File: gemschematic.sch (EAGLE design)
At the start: 15 parts, among them U7 STM32L073RZT6

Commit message: Add files via upload
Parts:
- added POWER: (no value), pinhead:PINHD-1X2
- added STLINK: 22-23-2041, con-molex:22-23-2041
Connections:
- removed net VDD: U7.VDD
- removed net VIN: BARO-1.S
- new net SWCLK: STLINK-3.S, U7.PA14
- new net SWIO: STLINK-2.S, U7.PA13
- net GND: now also POWER.2, STLINK-4.S
- net MISOLORA: now also U7.PA6; no longer U7.PC12
- net MOSILORA: now also U7.PA7; no longer U7.PC11
- net SCKLORA: now also U7.PA5; no longer U7.PC6
- net VCC: now also BARO-1.S, POWER.1, STLINK-1.S
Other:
- note added: "Stlink"
- moved on the sheet: DS18B20, PULLUP2
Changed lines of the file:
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@@
 <part name="BARO" library="con-molex" library_urn="urn:adsk.eagle:library:165" deviceset="22-23-2041" device="" package3d_urn="urn:adsk.eagle:package:8078635/1"/>
 <part name="GND6" library="supply1" library_urn="urn:adsk.eagle:library:371" deviceset="GND" device=""/>
+<part name="STLINK" library="con-molex" library_urn="urn:adsk.eagle:library:165" deviceset="22-23-2041" device="" package3d_urn="urn:adsk.eagle:package:8078635/1"/>
+<part name="POWER" library="pinhead" library_urn="urn:adsk.eagle:library:325" deviceset="PINHD-1X2" device="" package3d_urn="urn:adsk.eagle:package:22435/2"/>
 </parts>
 <sheets>
@@
 <text x="185.42" y="149.86" size="1.778" layer="91">Bluetooth Jumpers</text>
 <text x="241.3" y="-22.86" size="1.778" layer="91">version 3</text>
+<text x="205.74" y="55.88" size="1.778" layer="91">Stlink</text>
 </plain>
 <instances>
@@
 <attribute name="VALUE" x="-48.26" y="78.74" size="1.778" layer="96" rot="R270"/>
 </instance>
-<instance part="DS18B20" gate="A" x="-12.7" y="142.24" smashed="yes">
-<attribute name="NAME" x="-19.05" y="147.955" size="1.778" layer="95"/>
-<attribute name="VALUE" x="-19.05" y="134.62" size="1.778" layer="96"/>
-</instance>
-<instance part="GND4" gate="1" x="-33.02" y="139.7" smashed="yes" rot="R270">
-<attribute name="VALUE" x="-35.56" y="142.24" size="1.778" layer="96" rot="R270"/>
-</instance>
-<instance part="PULLUP2" gate="G$1" x="-38.1" y="144.78" smashed="yes" rot="R90">
-<attribute name="NAME" x="-39.5986" y="140.97" size="1.778" layer="95" rot="R90"/>
-<attribute name="VALUE" x="-34.798" y="140.97" size="1.778" layer="96" rot="R90"/>
-<attribute name="PULLUP" x="-38.1" y="144.78" size="1.778" layer="96" rot="R90" display="off"/>
+<instance part="DS18B20" gate="A" x="17.78" y="139.7" smashed="yes">
+<attribute name="NAME" x="11.43" y="145.415" size="1.778" layer="95"/>
+<attribute name="VALUE" x="11.43" y="132.08" size="1.778" layer="96"/>
+</instance>
+<instance part="GND4" gate="1" x="-2.54" y="137.16" smashed="yes" rot="R270">
+<attribute name="VALUE" x="-5.08" y="139.7" size="1.778" layer="96" rot="R270"/>
+</instance>
+<instance part="PULLUP2" gate="G$1" x="-7.62" y="142.24" smashed="yes" rot="R90">
+<attribute name="NAME" x="-9.1186" y="138.43" size="1.778" layer="95" rot="R90"/>
+<attribute name="VALUE" x="-4.318" y="138.43" size="1.778" layer="96" rot="R90"/>
+<attribute name="PULLUP" x="-7.62" y="142.24" size="1.778" layer="96" rot="R90" display="off"/>
 </instance>
 <instance part="BLUETOOTH" gate="-1" x="205.74" y="139.7" smashed="yes">
@@
 <instance part="GND6" gate="1" x="154.94" y="45.72" smashed="yes" rot="R270">
 <attribute name="VALUE" x="152.4" y="48.26" size="1.778" layer="96" rot="R270"/>
+</instance>
+<instance part="STLINK" gate="-1" x="215.9" y="48.26" smashed="yes">
+<attribute name="NAME" x="218.44" y="47.498" size="1.524" layer="95"/>
+</instance>
+<instance part="STLINK" gate="-2" x="215.9" y="45.72" smashed="yes">
+<attribute name="NAME" x="218.44" y="44.958" size="1.524" layer="95"/>
+</instance>
+<instance part="STLINK" gate="-3" x="215.9" y="43.18" smashed="yes">
+<attribute name="NAME" x="218.44" y="42.418" size="1.524" layer="95"/>
+</instance>
+<instance part="STLINK" gate="-4" x="215.9" y="40.64" smashed="yes">
+<attribute name="NAME" x="218.44" y="39.878" size="1.524" layer="95"/>
+</instance>
+<instance part="POWER" gate="G$1" x="167.64" y="12.7" smashed="yes">
+<attribute name="NAME" x="161.29" y="18.415" size="1.778" layer="95"/>
+<attribute name="VALUE" x="161.29" y="7.62" size="1.778" layer="96"/>
 </instance>
 </instances>
@@
 <segment>
 <pinref part="DS18B20" gate="A" pin="1"/>
-<wire x1="-15.24" y1="144.78" x2="-30.48" y2="144.78" width="0.1524" layer="91"/>
-<label x="-30.48" y="144.78" size="1.778" layer="95"/>
-<wire x1="-30.48" y1="144.78" x2="-30.48" y2="149.86" width="0.1524" layer="91"/>
-<wire x1="-30.48" y1="149.86" x2="-38.1" y2="149.86" width="0.1524" layer="91"/>
+<wire x1="15.24" y1="142.24" x2="0" y2="142.24" width="0.1524" layer="91"/>
+<label x="0" y="142.24" size="1.778" layer="95"/>
+<wire x1="0" y1="142.24" x2="0" y2="147.32" width="0.1524" layer="91"/>
+<wire x1="0" y1="147.32" x2="-7.62" y2="147.32" width="0.1524" layer="91"/>
 <pinref part="PULLUP2" gate="G$1" pin="2"/>
-<wire x1="-38.1" y1="149.86" x2="-43.18" y2="149.86" width="0.1524" layer="91"/>
-<junction x="-38.1" y="149.86"/>
+<wire x1="-7.62" y1="147.32" x2="-12.7" y2="147.32" width="0.1524" layer="91"/>
+<junction x="-7.62" y="147.32"/>
 </segment>
 <segment>
@@
 <wire x1="203.2" y1="132.08" x2="187.96" y2="132.08" width="0.1524" layer="91"/>
 <label x="187.96" y="132.08" size="1.778" layer="95"/>
+</segment>
+<segment>
+<pinref part="STLINK" gate="-1" pin="S"/>
+<wire x1="213.36" y1="48.26" x2="205.74" y2="48.26" width="0.1524" layer="91"/>
+<label x="205.74" y="48.26" size="1.778" layer="95"/>
+</segment>
+<segment>
+<pinref part="BARO" gate="-1" pin="S"/>
+<wire x1="167.64" y1="48.26" x2="157.48" y2="48.26" width="0.1524" layer="91"/>
+<label x="157.48" y="48.26" size="1.778" layer="95"/>
+</segment>
+<segment>
+<pinref part="POWER" gate="G$1" pin="1"/>
+<wire x1="165.1" y1="15.24" x2="154.94" y2="15.24" width="0.1524" layer="91"/>
+<label x="154.94" y="15.24" size="1.778" layer="95"/>
 </segment>
 </net>
@@
 <segment>
 <pinref part="DS18B20" gate="A" pin="3"/>
-<wire x1="-15.24" y1="139.7" x2="-30.48" y2="139.7" width="0.1524" layer="91"/>
+<wire x1="15.24" y1="137.16" x2="0" y2="137.16" width="0.1524" layer="91"/>
 <pinref part="GND4" gate="1" pin="GND"/>
 </segment>
@@
 <wire x1="167.64" y1="45.72" x2="157.48" y2="45.72" width="0.1524" layer="91"/>
 <pinref part="GND6" gate="1" pin="GND"/>
+</segment>
+<segment>
+<pinref part="STLINK" gate="-4" pin="S"/>
+<wire x1="213.36" y1="40.64" x2="205.74" y2="40.64" width="0.1524" layer="91"/>
+<label x="205.74" y="40.64" size="1.778" layer="95"/>
+</segment>
+<segment>
+<pinref part="POWER" gate="G$1" pin="2"/>
+<wire x1="165.1" y1="12.7" x2="154.94" y2="12.7" width="0.1524" layer="91"/>
+<label x="154.94" y="12.7" size="1.778" layer="95"/>
 </segment>
 </net>
@@
 </segment>
 </net>
-<net name="VDD" class="0">
-<segment>
-<pinref part="U7" gate="G$1" pin="VDD"/>
-<wire x1="96.52" y1="139.7" x2="111.76" y2="139.7" width="0.1524" layer="91"/>
-<label x="106.68" y="139.7" size="1.778" layer="95"/>
-</segment>
-</net>
 <net name="PA0LDR" class="0">
 <segment>
@@
 </segment>
 <segment>
-<pinref part="U7" gate="G$1" pin="PC6"/>
-<wire x1="96.52" y1="101.6" x2="111.76" y2="101.6" width="0.1524" layer="91"/>
-<label x="106.68" y="101.6" size="1.778" layer="95"/>
+<pinref part="U7" gate="G$1" pin="PA5"/>
+<wire x1="45.72" y1="104.14" x2="30.48" y2="104.14" width="0.1524" layer="91"/>
+<label x="30.48" y="104.14" size="1.778" layer="95"/>
 </segment>
 </net>
@@
 </segment>
 <segment>
-<pinref part="U7" gate="G$1" pin="PC12"/>
-<wire x1="96.52" y1="86.36" x2="111.76" y2="86.36" width="0.1524" layer="91"/>
-<label x="106.68" y="86.36" size="1.778" layer="95"/>
+<pinref part="U7" gate="G$1" pin="PA6"/>
+<wire x1="45.72" y1="101.6" x2="30.48" y2="101.6" width="0.1524" layer="91"/>
+<label x="30.48" y="101.6" size="1.778" layer="95"/>
 </segment>
 </net>
@@
 </segment>
 <segment>
-<pinref part="U7" gate="G$1" pin="PC11"/>
-<wire x1="96.52" y1="88.9" x2="111.76" y2="88.9" width="0.1524" layer="91"/>
-<label x="106.68" y="88.9" size="1.778" layer="95"/>
+<pinref part="U7" gate="G$1" pin="PA7"/>
+<wire x1="45.72" y1="99.06" x2="30.48" y2="99.06" width="0.1524" layer="91"/>
+<label x="30.48" y="99.06" size="1.778" layer="95"/>
 </segment>
 </net>
@@
 <segment>
 <pinref part="DS18B20" gate="A" pin="2"/>
-<wire x1="-15.24" y1="142.24" x2="-35.56" y2="142.24" width="0.1524" layer="91"/>
-<label x="-30.48" y="142.24" size="1.778" layer="95"/>
-<wire x1="-35.56" y1="142.24" x2="-35.56" y2="139.7" width="0.1524" layer="91"/>
+<wire x1="15.24" y1="139.7" x2="-5.08" y2="139.7" width="0.1524" layer="91"/>
+<label x="0" y="139.7" size="1.778" layer="95"/>
+<wire x1="-5.08" y1="139.7" x2="-5.08" y2="137.16" width="0.1524" layer="91"/>
 <pinref part="PULLUP2" gate="G$1" pin="1"/>
-<wire x1="-35.56" y1="139.7" x2="-38.1" y2="139.7" width="0.1524" layer="91"/>
-<wire x1="-38.1" y1="139.7" x2="-43.18" y2="139.7" width="0.1524" layer="91"/>
-<junction x="-38.1" y="139.7"/>
+<wire x1="-5.08" y1="137.16" x2="-7.62" y2="137.16" width="0.1524" layer="91"/>
+<wire x1="-7.62" y1="137.16" x2="-12.7" y2="137.16" width="0.1524" layer="91"/>
+<junction x="-7.62" y="137.16"/>
 </segment>
 <segment>
@@
 </segment>
 </net>
-<net name="VIN" class="0">
-<segment>
-<pinref part="BARO" gate="-1" pin="S"/>
-<wire x1="167.64" y1="48.26" x2="157.48" y2="48.26" width="0.1524" layer="91"/>
-<label x="157.48" y="48.26" size="1.778" layer="95"/>
-</segment>
-</net>
+<net name="SWIO" class="0">
+<segment>
+<pinref part="U7" gate="G$1" pin="PA13"/>
+<wire x1="45.72" y1="83.82" x2="30.48" y2="83.82" width="0.1524" layer="91"/>
+<label x="30.48" y="83.82" size="1.778" layer="95"/>
+</segment>
+<segment>
+<pinref part="STLINK" gate="-2" pin="S"/>
+<wire x1="213.36" y1="45.72" x2="205.74" y2="45.72" width="0.1524" layer="91"/>
+<label x="205.74" y="45.72" size="1.778" layer="95"/>
+</segment>
+</net>
+<net name="SWCLK" class="0">
+<segment>
+<pinref part="U7" gate="G$1" pin="PA14"/>
+<wire x1="45.72" y1="81.28" x2="30.48" y2="81.28" width="0.1524" layer="91"/>
+<label x="30.48" y="81.28" size="1.778" layer="95"/>
+</segment>
+<segment>
+<pinref part="STLINK" gate="-3" pin="S"/>
+<wire x1="213.36" y1="43.18" x2="205.74" y2="43.18" width="0.1524" layer="91"/>
+<label x="205.74" y="43.18" size="1.778" layer="95"/>
+</segment>
+</net>

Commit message: Add files via upload
added butons
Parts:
- added LEDRESISTOR: 510 Ohm, adafruit:R-US_0204/2V
- added RESETBUTTON, USERBUTTON: (no value), adafruit:40-XX
- added USERLED: (no value), adafruit:LED3MM
- BLUETOOTH: value 87438-06 -> (none); device con-molex:87438-06 -> adafruit:PINHD-1X6
- STLINK: value 22-23-2041 -> (none); device con-molex:22-23-2041 -> adafruit:PINHD-1X6
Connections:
- removed net !RESET: GPS1JUMPER.6
- removed net 3.3V: GPS1JUMPER.2
- removed net ANT: LORANT.1
- removed net IO18: LORA2JUMPER.5
- removed net IO19: LORA2JUMPER.6
- removed net IO23: LORA2JUMPER.7
- removed net IO25: LORA1JUMPER.5
- removed net IO27: LORA1JUMPER.4
- removed net IO4: LORA2JUMPER.3
- removed net IO5: LORA2JUMPER.4
- removed net MISOLORA: LORA1JUMPER.2, U7.PA6
- removed net MOSILORA: LORA1JUMPER.1, U7.PA7
- removed net RESET: LORA1JUMPER.6
- removed net RXI: LORA2JUMPER.8
- removed net SCKLORA: LORA1JUMPER.3, U7.PA5
- removed net SCL: LORA2JUMPER.2
- removed net SDA: LORA2JUMPER.1
- removed net SWCLK: STLINK-3.S, U7.PA14
- removed net SWIO: STLINK-2.S, U7.PA13
- removed net TXO: LORA2JUMPER.9
- removed net WAKEUP: GPS2JUMPER.6
- new net LED: LEDRESISTOR.2, U7.PA5
- new net N$1: LEDRESISTOR.1, USERLED.C
- new net NRST: RESETBUTTON.P, RESETBUTTON.P1, STLINK.5, U7.NRST
- new net SWCLKSTLINK: STLINK.2, U7.PA14
- new net SWDIOSTLINK: STLINK.4, U7.PA13
- new net SWOSTLINK: STLINK.6, U7.PB3
- new net USERBUTTON: U7.PC13, USERBUTTON.P, USERBUTTON.P1
- net BTRX: now also BLUETOOTH.2; no longer BLUETOOTH-2.S
- net BTTX: now also BLUETOOTH.3; no longer BLUETOOTH-3.S
- net GND: now also BLUETOOTH.5, RESETBUTTON.S, RESETBUTTON.S1, STLINK.3, U7.BOOT0, USERBUTTON.S, USERBUTTON.S1; no longer BLUETOOTH-5.S, STLINK-4.S
- net VCC: now also BLUETOOTH.4; no longer BLUETOOTH-4.S, STLINK-1.S
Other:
- note added: "LED"
- note added: "Power"

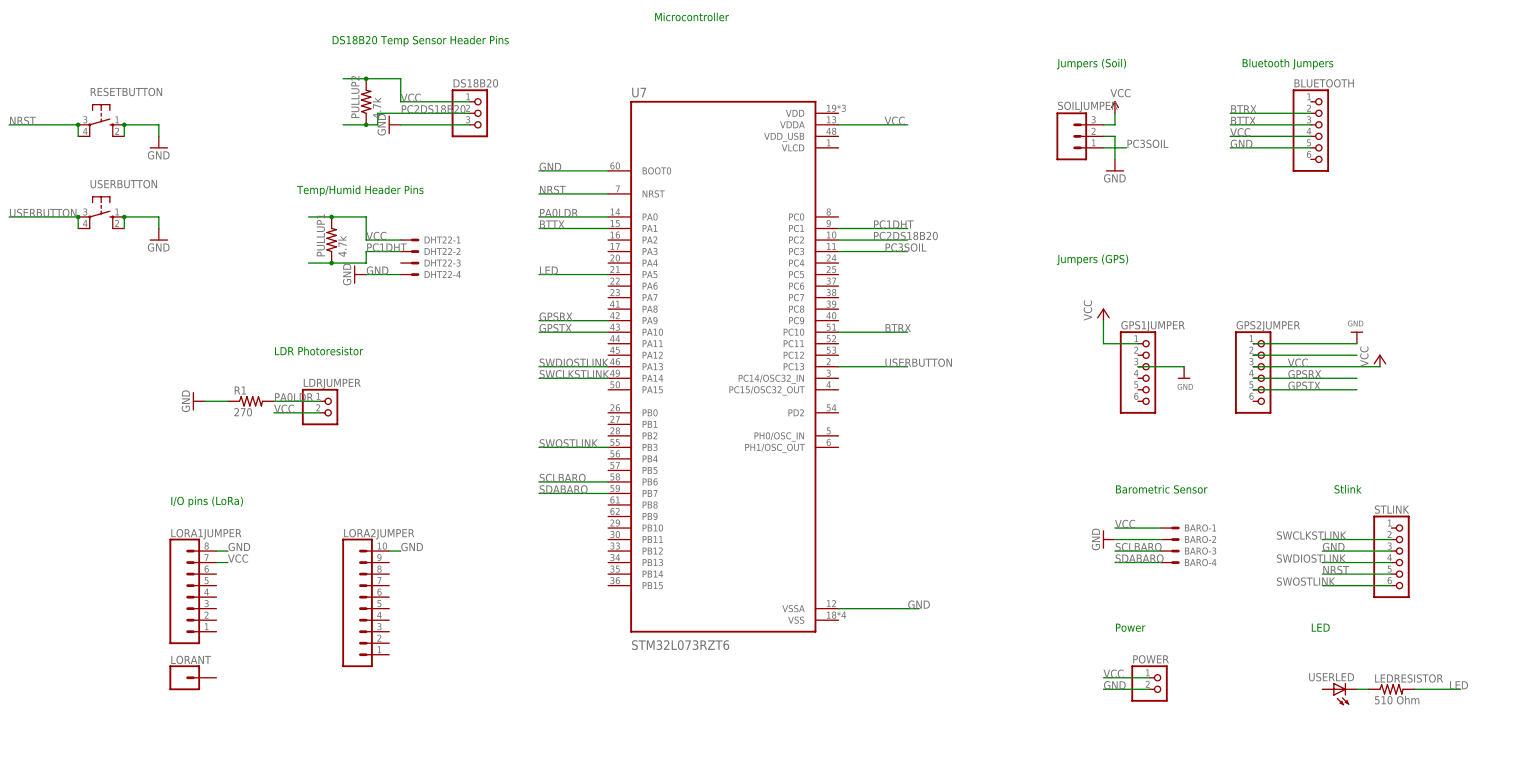
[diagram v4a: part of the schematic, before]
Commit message: added smd parts
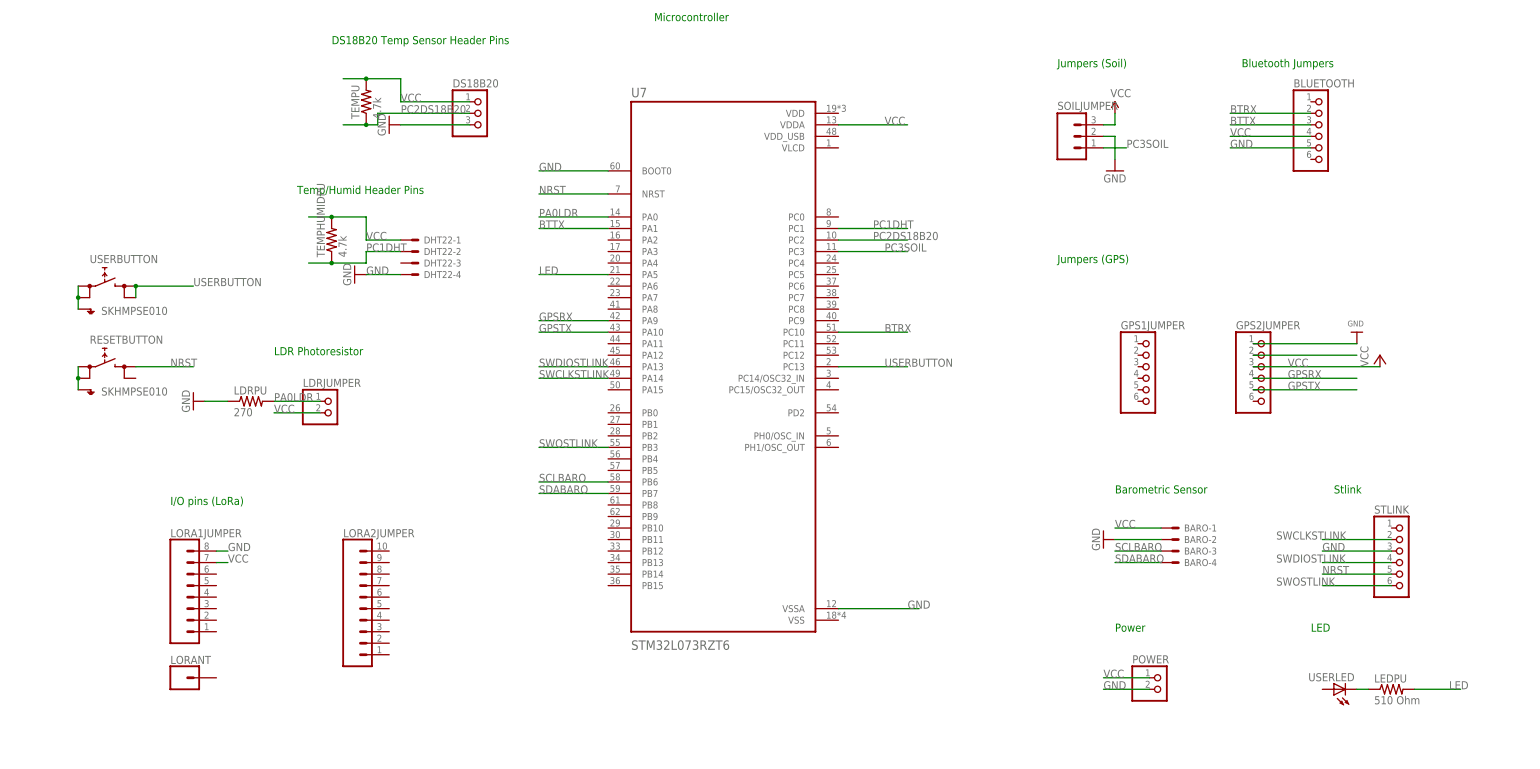
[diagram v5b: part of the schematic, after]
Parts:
- removed LEDRESISTOR: 510 Ohm, adafruit:R-US_0204/2V
- removed PULLUP1, PULLUP2: 4.7k, adafruit:R-US_0204/2V
- removed R1: 270, adafruit:R-US_0204/2V
- added LDRPU: 270, adafruit:R-US_M0805
- added LEDPU: 510 Ohm, adafruit:R-US_M0805
- added TEMPHUMIDPU, TEMPU: 4.7k, adafruit:R-US_M0805
- RESETBUTTON, USERBUTTON: value (none) -> SKHMPSE010; device adafruit:40-XX -> switch:SKHMPSE010
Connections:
- new net N$2: USERBUTTON.1.1, USERBUTTON.1.2, USERBUTTON.SH
- new net N$4: RESETBUTTON.1.1, RESETBUTTON.1.2, RESETBUTTON.SH
- net GND: now also LDRPU.1; no longer GPS1JUMPER.3, LORA2JUMPER.10, R1.1, RESETBUTTON.S, RESETBUTTON.S1, USERBUTTON.S, USERBUTTON.S1
- net LED: now also LEDPU.2; no longer LEDRESISTOR.2
- net N$1: now also LEDPU.1; no longer LEDRESISTOR.1
- net NRST: now also RESETBUTTON.2.1; no longer RESETBUTTON.P, RESETBUTTON.P1
- net PA0LDR: now also LDRPU.2; no longer R1.2
- net PC1DHT: now also TEMPHUMIDPU.1; no longer PULLUP1.1
- net PC2DS18B20: now also TEMPU.1; no longer PULLUP2.1
- net USERBUTTON: now also USERBUTTON.2.1, USERBUTTON.2.2; no longer USERBUTTON.P, USERBUTTON.P1
- net VCC: now also TEMPHUMIDPU.2, TEMPU.2; no longer GPS1JUMPER.1, PULLUP1.2, PULLUP2.2
